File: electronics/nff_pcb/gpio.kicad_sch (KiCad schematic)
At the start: 20 parts, among them U10 CH340C, U2 A33, Y1 24Mhz, Y2 32.768khz

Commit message: R0.1 released.
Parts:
- U10: MPN (none) -> CH340C
- U2: MPN A33 -> "Allwinner A33" or "Allwinner R16"
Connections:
- net CLK renamed SDC1.CLK
- net CMD renamed SDC1.CMD
- net D0 renamed SDC1.D0
- net D1 renamed SDC1.D1
- net D2 renamed SDC1.D2
- net D3 renamed SDC1.D3
- net SD_CLK renamed SDC0.CLK
- net SD_CMD renamed SDC0.CMD
- net SD_DAT0 renamed SDC0.D0
- net SD_DAT1 renamed SDC0.D1
- net SD_DAT2 renamed SDC0.D2
- net SD_DAT3 renamed SDC0.D3
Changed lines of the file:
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@@
 		(company "Interrupt Labs")
 	)
+	(bus_alias "SDC0"
+		(members "SDC0.D[3..0]" "SDC0.CLK" "SDC0.CMD")
+	)
 	(bus_alias "USB"
 		(members "D+" "D-")
@@
 	)
 	(bus_entry
+		(at 74.93 77.47)
+		(size 2.54 -2.54)
+		(stroke
+			(width 0)
+			(type default)
+		)
+	)
+	(bus_entry
 		(at 163.83 57.15)
 		(size 2.54 2.54)
@@
 	)
 	(bus_entry
+		(at 74.93 80.01)
+		(size 2.54 -2.54)
+		(stroke
+			(width 0)
+			(type default)
+		)
+	)
+	(bus_entry
 		(at 163.83 72.39)
 		(size 2.54 2.54)
@@
 	(wire
 		(pts
-			(xy 53.34 80.01) (xy 67.31 80.01)
+			(xy 53.34 80.01) (xy 74.93 80.01)
 		)
 		(stroke
@@
 	(bus
 		(pts
+			(xy 77.47 77.47) (xy 77.47 80.01)
+		)
+		(stroke
+			(width 0)
+			(type default)
+		)
+	)
+	(bus
+		(pts
 			(xy 77.47 87.63) (xy 77.47 90.17)
 		)
@@
 		)
 	)
+	(bus
+		(pts
+			(xy 77.47 74.93) (xy 77.47 77.47)
+		)
+		(stroke
+			(width 0)
+			(type default)
+		)
+	)
 	(wire
 		(pts
@@
 	(wire
 		(pts
-			(xy 67.31 77.47) (xy 53.34 77.47)
+			(xy 53.34 77.47) (xy 74.93 77.47)
 		)
 		(stroke
@@
 	(bus
 		(pts
-			(xy 77.47 72.39) (xy 77.47 80.01)
+			(xy 77.47 72.39) (xy 77.47 74.93)
 		)
 		(stroke
@@
 		)
 	)
-	(label "D3"
+	(label "SDC1.D3"
 		(at 57.15 102.87 0)
 		(fields_autoplaced yes)
@@
 		)
 	)
-	(label "SD_DAT1"
+	(label "SDC0.D1"
 		(at 57.15 72.39 0)
 		(fields_autoplaced yes)
@@
 		)
 	)
-	(label "CMD"
+	(label "SDC1.CMD"
 		(at 57.15 92.71 0)
 		(fields_autoplaced yes)
@@
 	(label "D+"
 		(at 113.03 151.13 0)
+		(fields_autoplaced yes)
 		(effects
 			(font
@@
 		)
 	)
-	(label "SD_CMD"
+	(label "SDC0.CMD"
 		(at 57.15 80.01 0)
 		(fields_autoplaced yes)
@@
 		)
 	)
-	(label "SD_DAT2"
+	(label "SDC0.D2"
 		(at 57.15 85.09 0)
 		(fields_autoplaced yes)
@@
 		)
 	)
-	(label "SD_DAT0"
+	(label "SDC0.D0"
 		(at 57.15 74.93 0)
 		(fields_autoplaced yes)
@@
 		)
 	)
-	(label "CLK"
+	(label "SDC1.CLK"
 		(at 57.15 90.17 0)
 		(fields_autoplaced yes)
@@
 		)
 	)
-	(label "D1"
+	(label "SDC1.D1"
 		(at 57.15 97.79 0)
 		(fields_autoplaced yes)
@@
 		)
 	)
-	(label "D2"
+	(label "SDC1.D2"
 		(at 57.15 100.33 0)
 		(fields_autoplaced yes)
@@
 		)
 	)
-	(label "SD_CLK"
+	(label "SDC0.CLK"
 		(at 57.15 77.47 0)
 		(fields_autoplaced yes)
@@
 		)
 	)
-	(label "D0"
+	(label "SDC1.D0"
 		(at 57.15 95.25 0)
 		(fields_autoplaced yes)
@@
 		)
 	)
-	(label "SD_DAT3"
+	(label "SDC0.D3"
 		(at 57.15 82.55 0)
 		(fields_autoplaced yes)
@@
 	(label "D-"
 		(at 113.03 153.67 0)
+		(fields_autoplaced yes)
 		(effects
 			(font
@@
 		)
 	)
-	(hierarchical_label "SD_CLK"
-		(shape input)
-		(at 67.31 77.47 0)
-		(fields_autoplaced yes)
-		(effects
-			(font
-				(size 1.27 1.27)
-			)
-			(justify left)
-		)
-	)
 	(hierarchical_label "USB-DP1"
 		(shape input)
@@
 		)
 	)
-	(hierarchical_label "{SDC}"
+	(hierarchical_label "{SDC1}"
 		(shape input)
 		(at 81.28 86.36 0)
@@
 		)
 	)
-	(hierarchical_label "SD_DAT[0..3]"
+	(hierarchical_label "{SDC0}"
 		(shape input)
 		(at 81.28 67.31 0)
@@
 		)
 	)
-	(hierarchical_label "SD_CMD"
-		(shape input)
-		(at 67.31 80.01 0)
-		(fields_autoplaced yes)
-		(effects
-			(font
-				(size 1.27 1.27)
-			)
-			(justify left)
-		)
-	)
 	(symbol
 		(lib_id "Allwinner_A33:A33")
@@
 			)
 		)
-		(property "MPN" "A33"
+		(property "MPN" "\"Allwinner A33\" or \"Allwinner R16\""
 			(at 41.91 14.859 0)
 			(effects
@@
 			)
 		)
-		(property "MPN" "A33"
+		(property "MPN" "\"Allwinner A33\" or \"Allwinner R16\""
 			(at 191.77 30.099 0)
 			(effects
@@
 			(at 101.6 153.67 0)
 			(effects
+				(font
+					(size 1.27 1.27)
+				)
+				(hide yes)
+			)
+		)
+		(property "MPN" "CH340C"
+			(at 101.6 153.67 0)
+			(effects

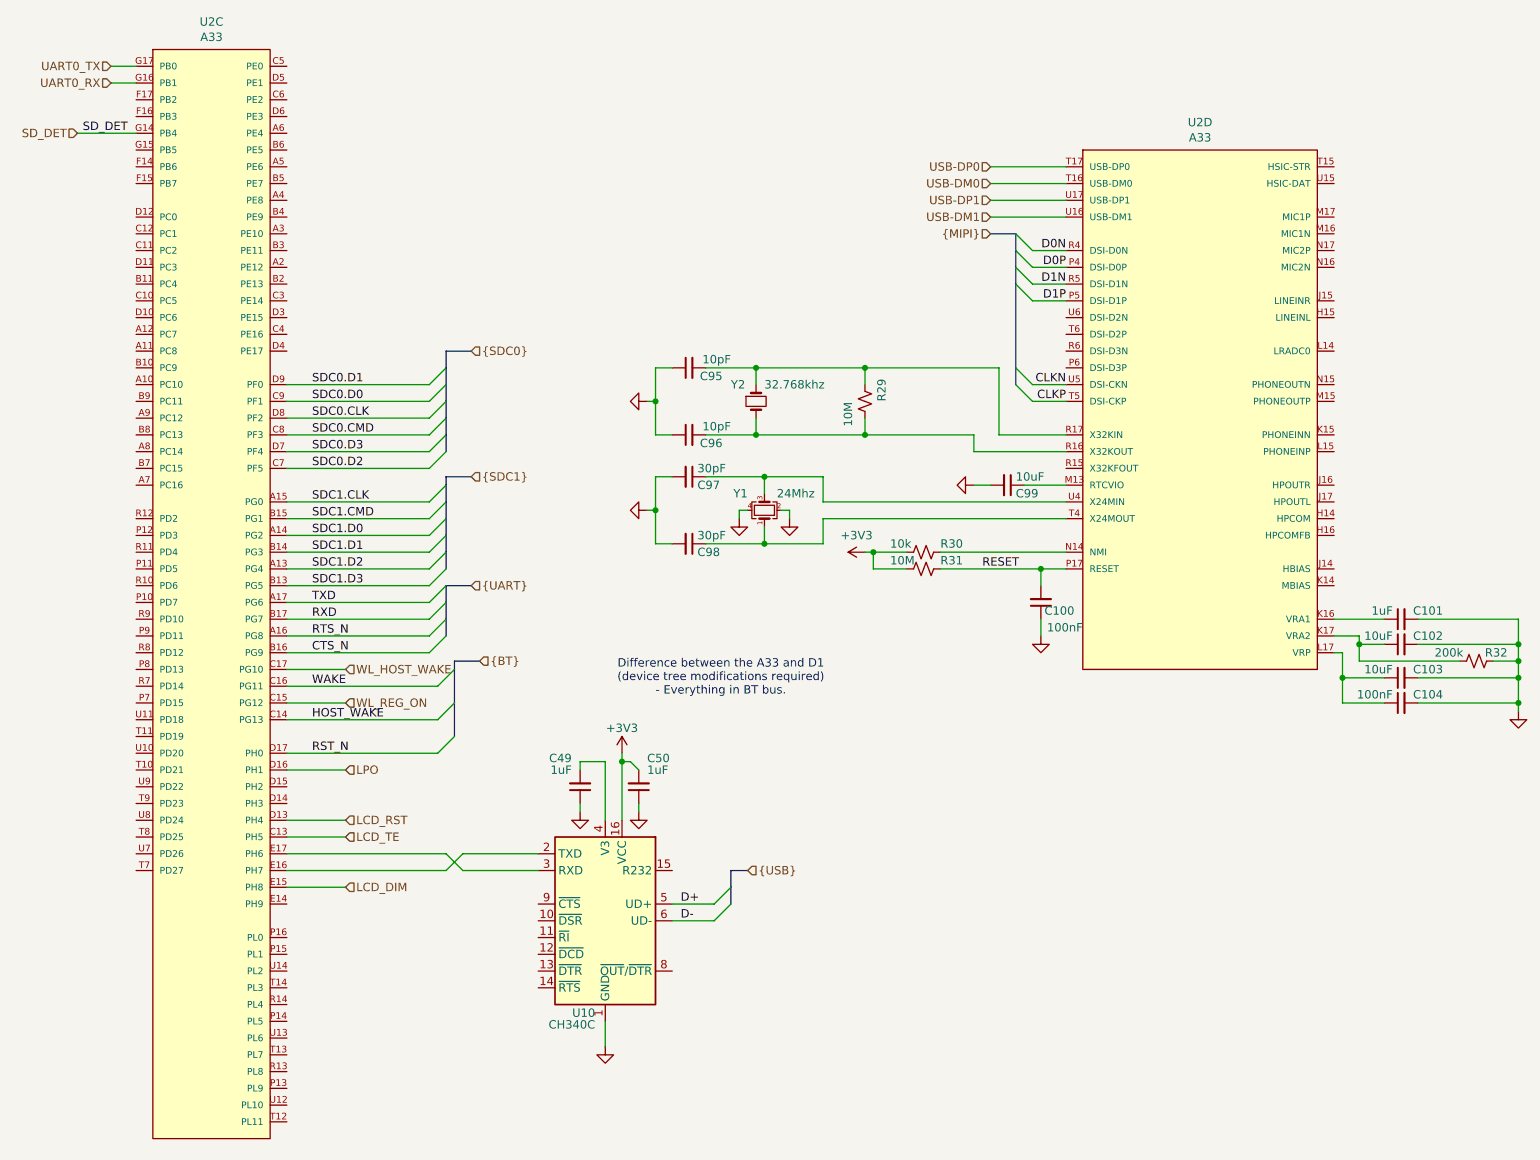
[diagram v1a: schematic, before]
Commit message: “or” the 5V line, “or” the UART bus, reroute the PWM line to be actually PWM, Reset button., Decoup caps over USB.
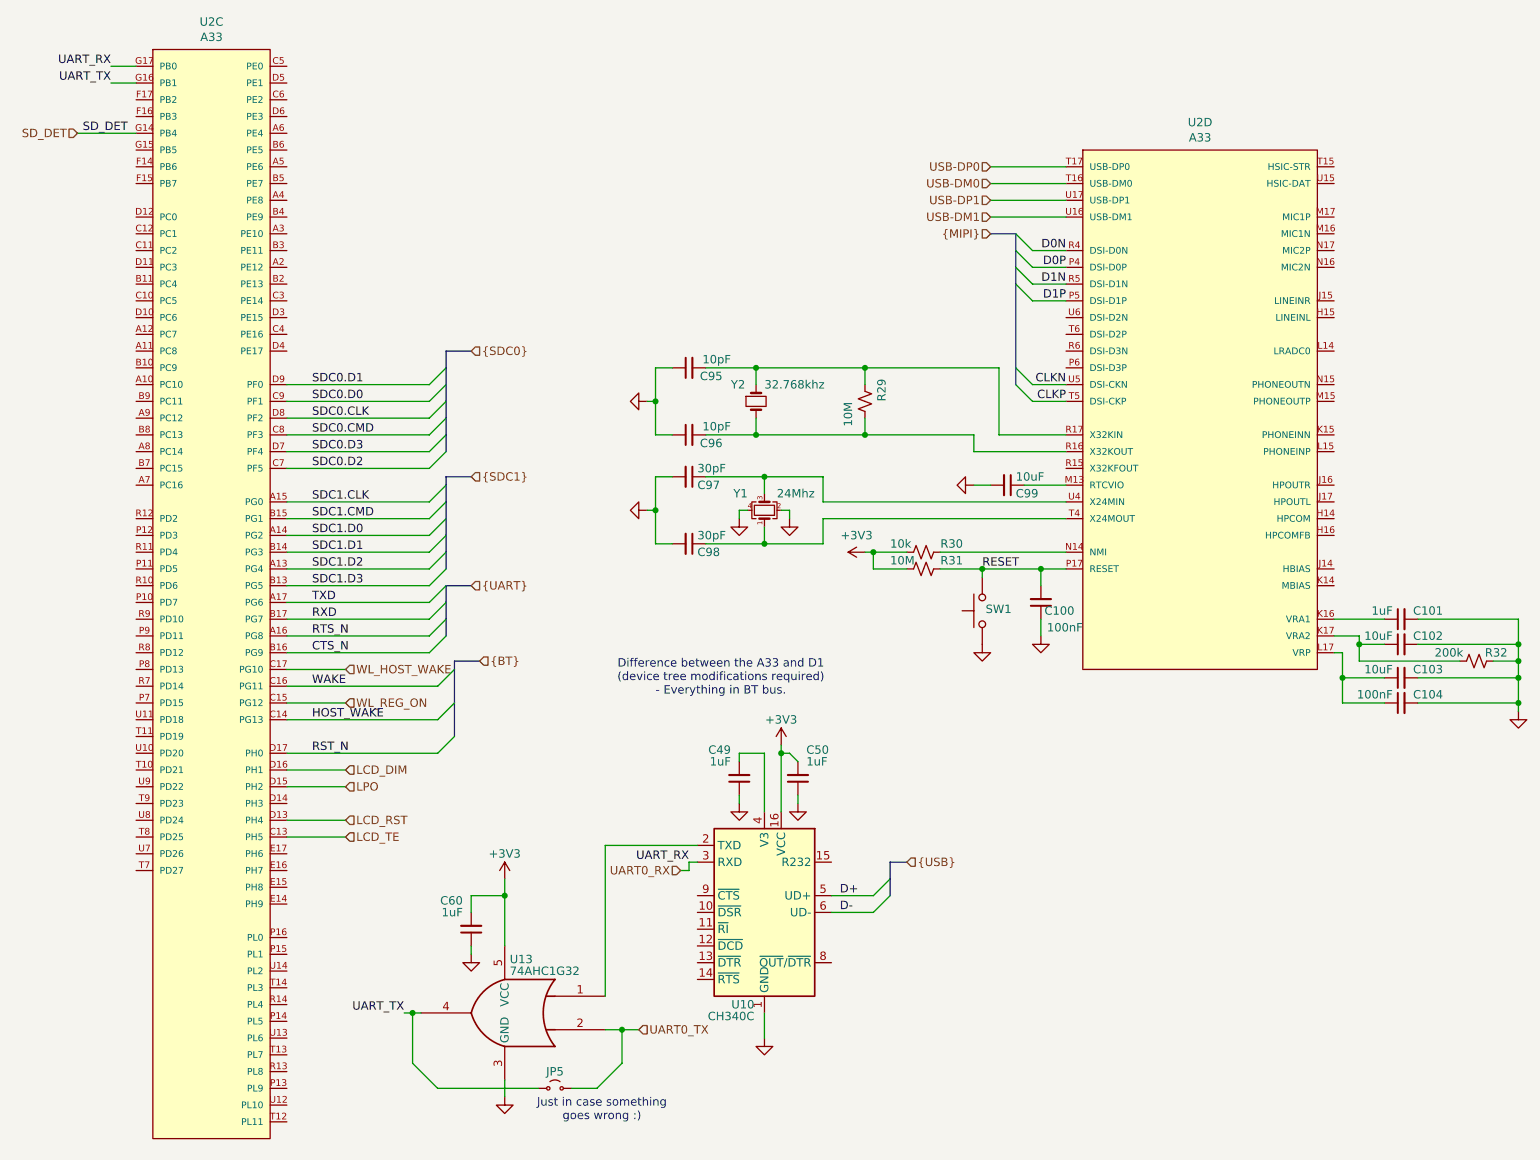
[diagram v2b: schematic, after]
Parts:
- added C60: 1uF, Capacitor_SMD:C_0402_1005Metric, symbol Device:C_Small
- added JP5: Jumper_2_Small_Open, Jumper:SolderJumper-2_P1.3mm_Open_RoundedPad1.0x1.5mm, symbol Jumper:Jumper_2_Small_Open
- added SW1: SW_Push, Button_Switch_SMD:SW_SPST_TL3305A, symbol Switch:SW_Push
- added U13: 74AHC1G32, Package_TO_SOT_SMD:SOT-353_SC-70-5, symbol 74xGxx:74AHC1G32
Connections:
- net +3V3: now also C60.2, U13.5 (VCC)
- net GND: now also C60.1, SW1.1, U13.3 (GND)
- net LCD_DIM: now also U2.D16 (PH1); no longer U2.E15 (PH8)
- net LPO: now also U2.D15 (PH2); no longer U2.D16 (PH1)
- net RESET: now also SW1.2
- net UART0_RX: now also U10.3 (RXD), U2.G17 (PB0); no longer U2.G16 (PB1)
- net UART0_TX: now also JP5.2 (B), U13.2; no longer U2.G17 (PB0)
- net at U2.E16 (PH7): no longer U10.2 (TXD)
- net at U2.E17 (PH6): no longer U10.3 (RXD)
- new net: U10.2 (TXD), U13.1
- new net UART_TX: JP5.1 (A), U13.4, U2.G16 (PB1)
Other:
- note added: "Just in case something goes wrong :)"
- moved on the sheet: C49, C50, U10

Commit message: R2 Released
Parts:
- added D1: Green, LED_SMD:LED_0603_1608Metric, symbol Device:LED
- added R45: 1k, Resistor_SMD:R_0402_1005Metric, symbol Device:R_Small_US
- JP5: now left out of the parts list
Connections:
- net GND: now also D1.1 (K)
- net at U2.U14 (PL2): now also R45.1
- new net: D1.2 (A), R45.2
